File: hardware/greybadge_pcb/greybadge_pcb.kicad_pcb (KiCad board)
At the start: 2 copper layers, 105.3 x 99 mm, 64 parts, among them J1 CONN_01X14, J2 CONN_01X14, J3 USB_OTG, J4 Conn_02x08_Odd_Even, J5 Conn_02x03_Odd_Even, SW1 SW_Push, SW3 SW_Push, U1 iCE40-LP8K-CM81, U2 MIC5504-3.3YM5-TR, U3 DSC6001CI2A-016.0000T, U4 MIC5365-1.2YC5-TR, U5 AT25SF081-SSHD-B

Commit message: feat: linking tinyfpga stuff
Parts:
- C10: value 100nF -> 1uF
- C14: value 10nF -> 100nF
- C15: value 10nF -> 1uF
- C2, C3, C4: value 1uF -> 100nF
- C7, C9: value 100nF -> 10nF
- R1: value 1.5k -> 100
- R2: value 68 -> 1.5k
- R4: value 100 -> 68
- R5: value 10k -> 270
- R8: value 270 -> 10k
- U2: value MIC5504-3.3YM5-TR -> MIC5365-1.2YC5-TR
- moved C1 20.2 mm to (201.6, 79.9)
- moved C11 20.2 mm to (193.1, 90.1)
- moved C12 20.2 mm to (193.1, 90.9)
- moved C13 20.2 mm to (200.1, 90.2)
- moved C14 20.2 mm to (199.8, 88.4)
- moved C15 20.2 mm to (196.8, 87.0)
- moved C16 20.2 mm to (196.2, 94.4)
- moved C2 20.2 mm to (201.6, 83.5)
- moved C3 20.2 mm to (201.6, 85.9)
- moved C4 20.2 mm to (201.6, 82.3)
- moved C6 20.2 mm to (197.4, 96.1)
- moved C7 20.2 mm to (197.4, 93.7)
- moved C8 20.2 mm to (194.5, 93.8)
- moved C9 20.2 mm to (198.9, 93.5)
- moved D2 20.2 mm to (191.9, 79.4)
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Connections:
- C1 pad 1: (no net) -> +5V
- C1 pad 2: (no net) -> GND
- C10 pad 1: (no net) -> +3V3
- C10 pad 2: (no net) -> GND
- C11 pad 1: (no net) -> Net-(U3G-GNDPLL0)
- C11 pad 2: (no net) -> Net-(U3G-VCCPLL0)
- C12 pad 1: (no net) -> +3V3
- C12 pad 2: (no net) -> GND
- C13 pad 1: (no net) -> +3V3
- C13 pad 2: (no net) -> GND
- C14 pad 1: (no net) -> +3V3
- C14 pad 2: (no net) -> GND
- C15 pad 1: (no net) -> +1V2
- C15 pad 2: (no net) -> GND
- C16 pad 1: (no net) -> +3V3
- C16 pad 2: (no net) -> GND
- C2 pad 1: (no net) -> +3V3
- C2 pad 2: (no net) -> GND
- C3 pad 1: (no net) -> +3V3
- C3 pad 2: (no net) -> GND
- C4 pad 1: (no net) -> +1V2
- C4 pad 2: (no net) -> GND
- C7 pad 1: (no net) -> +1V2
- C7 pad 2: (no net) -> GND
- C9 pad 1: (no net) -> +1V2
- C9 pad 2: (no net) -> GND
- D1 pad 1: (no net) -> Net-(D1-K)
- D1 pad 2: (no net) -> +3V3
- D2 pad 1: (no net) -> Net-(D2-K)
- D2 pad 2: (no net) -> LED
- L1 pad 1: (no net) -> +5V
- L1 pad 2: (no net) -> Net-(J1-VBUS)
- R1 pad 1: (no net) -> Net-(U3G-VCCPLL0)
- R1 pad 2: (no net) -> +1V2
- R10 pad 1: (no net) -> +3V3
- R10 pad 2: (no net) -> SS
- R2 pad 1: (no net) -> Net-(J1-D+)
- R2 pad 2: (no net) -> USB_PU
- R3 pad 1: (no net) -> USB_P
- R3 pad 2: (no net) -> Net-(J1-D+)
- R4 pad 1: (no net) -> USB_N
- R4 pad 2: (no net) -> Net-(J1-D-)
- R5 pad 1: (no net) -> Net-(D1-K)
- R5 pad 2: (no net) -> GND
- R7 pad 1: (no net) -> +3V3
- R7 pad 2: (no net) -> 82
- R8 pad 1: (no net) -> +3V3
- R8 pad 2: (no net) -> 109
- SW1 pad 1: (no net) -> GND
- SW1 pad 2: (no net) -> CRESET_B
- TP1 pad 1: (no net) -> +1V2
- TP2 pad 1: (no net) -> 82
- TP3 pad 1: (no net) -> CRESET_B
- U2 pad 1: (no net) -> +3V3
- U2 pad 2: (no net) -> GND
- U2 pad 3: (no net) -> +3V3
- U2 pad 4: (no net) -> unconnected-(U2-NC-Pad4)
- U2 pad 5: (no net) -> +1V2
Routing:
- net (no net): track 699.3 -> 547.5 mm, vias 77 -> 41
- net GND: track 0.00 -> 43.9 mm, vias 0 -> 16
- net +1V2: track 0.00 -> 23.0 mm, vias 0 -> 3
- net SS: track 0.00 -> 20.3 mm, vias 0 -> 2
- net Net-(J1-D+): track 0.00 -> 17.0 mm, vias 0 -> 1
- net USB_P: track 0.00 -> 15.6 mm, vias 0 -> 1
- net LED: track 0.00 -> 13.4 mm, vias 0 -> 1
- net +3V3: track 0.00 -> 11.6 mm, vias 0 -> 8
- net Net-(J1-VBUS): track 0.00 -> 2.36 mm
- net Net-(D1-K): track 0.00 -> 1.84 mm, vias 0 -> 1
- net Net-(D2-K): track 0.00 -> 1.04 mm
- net Net-(U3G-VCCPLL0): track 0.00 -> 0.71 mm, vias 0 -> 1
- net 109: track 0.00 -> 0.63 mm, vias 0 -> 1
- net Net-(J1-D-): track 0.00 -> 0.42 mm, vias 0 -> 1
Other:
- board size 105.3 x 99 mm -> 124 x 99 mm

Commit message: feat: arrangement
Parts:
- moved J5 43.9 mm to (239.4, 77.4)
- moved C1 43.9 mm to (245.5, 78.5)
- moved C10 43.9 mm to (238.1, 81.9)
- moved C11 43.9 mm to (237.0, 88.7)
- moved C12 43.9 mm to (237.0, 89.5)
- moved C13 43.9 mm to (243.9, 88.7)
- moved C14 43.9 mm to (243.6, 87.0)
- moved C15 43.9 mm to (240.7, 85.5)
- moved C16 43.9 mm to (240.1, 93.0)
- moved C17 43.9 mm to (245.6, 75.5)
- moved C2 43.9 mm to (245.5, 82.1)
- moved C3 43.9 mm to (245.5, 84.5)
- moved C4 43.9 mm to (245.5, 80.9)
- moved C6 43.9 mm to (241.3, 94.7)
- moved C7 43.9 mm to (241.3, 92.2)
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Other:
- board size 124 x 99 mm -> 167.8 x 99 mm

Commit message: Update sch and pcb
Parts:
- added C18: 100n, Capacitor_SMD:C_0402_1005Metric, B.Cu at (94.1, 62.9)
- added C19: 4.7u, Capacitor_SMD:C_0402_1005Metric, B.Cu at (105.2, 61.9)
- added C20: 4.7u, Capacitor_SMD:C_0402_1005Metric, B.Cu at (103.5, 64.3)
- added C21: 4.7u, Capacitor_SMD:C_0402_1005Metric, B.Cu at (104.5, 64.3)
- added C22: 22pF, Capacitor_SMD:C_0402_1005Metric, B.Cu at (86.0, 68.7)
- added C23: 22pF, Capacitor_SMD:C_0402_1005Metric, B.Cu at (85.7, 65.2)
- added C24: 100n, Capacitor_SMD:C_0402_1005Metric, B.Cu at (106.0, 68.5)
- added C25: 100n, Capacitor_SMD:C_0402_1005Metric, B.Cu at (92.4, 68.8)
- added C26: 100n, Capacitor_SMD:C_0402_1005Metric, B.Cu at (97.7, 71.8)
- added C27: 100n, Capacitor_SMD:C_0402_1005Metric, B.Cu at (128.8, 53.5)
- added C28: 100n, Capacitor_SMD:C_0402_1005Metric, B.Cu at (110.7, 69.4)
- added C29: 100n, Capacitor_SMD:C_0402_1005Metric, B.Cu at (98.6, 61.0)
- added C30: 100n, Capacitor_SMD:C_0402_1005Metric, B.Cu at (102.7, 71.3)
- added C31: 100n, Capacitor_SMD:C_0402_1005Metric, B.Cu at (99.6, 61.0)
- added C32: 4.7u, Capacitor_SMD:C_0402_1005Metric, B.Cu at (99.7, 71.8)
- added C33: 100n, Capacitor_SMD:C_0402_1005Metric, B.Cu at (92.4, 66.2)
- added C34: 10u, Capacitor_SMD:C_0805_2012Metric, B.Cu at (130.5, 58.5)
- added C35: 10u, Capacitor_SMD:C_0805_2012Metric, B.Cu at (130.5, 55.5)
- added J6: SM03B-SRSS-TB, Connector_JST:JST_SH_SM03B-SRSS-TB_1x03-1MP_P1.00mm_Horizontal, B.Cu at (93.4, 46.3)
- added J7: USB_C_Receptacle_USB2.0, Connector_USB:USB_C_Receptacle_HRO_TYPE-C-31-M-12, B.Cu at (151.9, 61.1)
- added L2: 3.3u, footprints:L_pol_2016, B.Cu at (106.0, 64.3)
- added R11: DNF, Resistor_SMD:R_0402_1005Metric, B.Cu at (112.5, 78.7)
- added R12: 33, Resistor_SMD:R_0402_1005Metric, B.Cu at (104.0, 61.9)
- added R13: DNF, Resistor_SMD:R_0402_1005Metric, B.Cu at (112.5, 79.9)
- added R14: 0, Resistor_SMD:R_0402_1005Metric, B.Cu at (109.6, 80.0)
- added R15: 27R, Resistor_SMD:R_0402_1005Metric, B.Cu at (106.0, 67.1)
- added R16: 27R, Resistor_SMD:R_0402_1005Metric, B.Cu at (106.0, 66.1)
- added R17: 1k, Resistor_SMD:R_0402_1005Metric, B.Cu at (109.6, 81.2)
- added R18: 1k, Resistor_SMD:R_0402_1005Metric, B.Cu at (89.2, 65.5)
- added R19: 1k, Resistor_SMD:R_0402_1005Metric, B.Cu at (87.3, 62.5)
- added R20: 5k1, Resistor_SMD:R_0402_1005Metric, B.Cu at (144.8, 57.1)
- added R21: 5k1, Resistor_SMD:R_0402_1005Metric, B.Cu at (144.8, 65.3)
- added SW2: SW_Push, Button_Switch_SMD:SW_Push_1P1T_NO_Vertical_Wuerth_434133025816, B.Cu at (105.6, 83.0)
- added SW3: SW_Push, Button_Switch_SMD:SW_Push_1P1T_NO_Vertical_Wuerth_434133025816, B.Cu at (89.8, 59.9)
- added U6: W25Q128JVS, Package_SO:SOIC-8_5.3x5.3mm_P1.27mm, B.Cu at (108.3, 74.6)
- added U7: RP2350_60QFN, footprints:RP2350-QFN-60-1EP_7x7_P0.4mm_EP3.4x3.4mm_ThermalVias, B.Cu at (98.9, 66.5)
- added U8: NCP1117-3.3_SOT223, Package_TO_SOT_SMD:SOT-223-3_TabPin2, B.Cu at (137.7, 56.5)
- added Y1: 12Mhz, Crystal:Crystal_SMD_3225-4Pin_3.2x2.5mm, B.Cu at (87.6, 67.1)
- L1: footprint Inductors_SMD:L_0603 -> Inductor_SMD:L_0603_1608Metric
- renumbered C4 to C10, C7 to C11, C9 to C12, C12 to C13, C13 to C14, C14 to C15, C11 to C17, C15 to C3, C1 to C4, C10 to C6, C16 to C7, C2 to C8, C3 to C9, R2 to R1, R1 to R10, R3 to R2, R4 to R3, R5 to R4, R10 to R6, U2 to U4
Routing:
- net /rp2350/USB_D+: track 0.00 -> 43.5 mm
- net /rp2350/USB_D-: track 0.00 -> 43.3 mm
- net GND: track 43.9 -> 66.2 mm, vias 16 -> 25
- net /rp2350/GPIO0: track 0.00 -> 21.8 mm, vias 0 -> 2
- net +3V3: track 11.6 -> 31.3 mm, vias 8 -> 9
- net /rp2350/QSPI_SS: track 0.00 -> 17.0 mm
- net /rp2350/QSPI_SD1: track 0.00 -> 16.7 mm
- net /rp2350/QSPI_SD2: track 0.00 -> 12.5 mm
- net +1V1: track 0.00 -> 12.0 mm, vias 0 -> 5
- net /rp2350/XIN: track 0.00 -> 10.3 mm
- net /rp2350/QSPI_SD3: track 0.00 -> 8.64 mm
- net /rp2350/QSPI_SCLK: track 0.00 -> 7.19 mm
- net /rp2350/~{USB_BOOT}: track 0.00 -> 6.89 mm
- net (no net): track 547.5 -> 540.8 mm, vias 41 -> 40
- net /rp2350/XOUT: track 0.00 -> 6.34 mm
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- added copper zone on B.Cu, net +1V1
- added copper zone on B.Cu, net +3V3

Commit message: Update routing
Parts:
- moved C27 28.5 mm to (101.3, 61.0), turned to 90 degrees
- moved C34 9.96 mm to (140.5, 57.6), turned to 90 degrees
- moved U8 3.87 mm to (133.8, 56.5), turned to 180 degrees
- moved R19 2.94 mm to (85.7, 60.0), turned to 90 degrees
- moved C35 2.53 mm to (128.0, 55.6), turned to 90 degrees
- moved R21 2.27 mm to (144.5, 63.1)
- moved R20 2.17 mm to (144.5, 59.3)
- moved C18 2.15 mm to (95.3, 61.1)
- moved C26 1.35 mm to (97.4, 73.1)
- moved C32 1.34 mm to (100.0, 73.1)
- moved C30 0.91 mm to (103.5, 71.8), turned to -90 degrees
- moved SW3 0.65 mm to (89.4, 59.4), turned to 0 degrees
- moved C29 0.57 mm to (98.6, 60.5)
- moved C31 0.57 mm to (99.6, 60.5)
- moved C25 0.27 mm to (92.1, 68.8)
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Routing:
- net GND: track 66.2 -> 101.1 mm, vias 25 -> 38
- net VBUS: track 0.00 -> 17.9 mm, vias 0 -> 2
- net +3V3: track 31.3 -> 44.2 mm
- net /rp2350/RUN: track 2.90 -> 14.6 mm
- net /rp2350/GPIO16: track 0.00 -> 11.4 mm
- net /rp2350/GPIO17: track 0.00 -> 11.3 mm
- net +1V1: track 12.0 -> 22.9 mm, vias 5 -> 8
- net /rp2350/GPIO18: track 0.00 -> 10.1 mm
- net /rp2350/GPIO8: track 0.00 -> 7.39 mm
- net /rp2350/GPIO9: track 0.00 -> 6.83 mm
- net Net-(R19-Pad1): track 0.00 -> 5.91 mm
- net /rp2350/GPIO1: track 0.00 -> 5.85 mm
- net /rp2350/GPIO2: track 0.00 -> 5.81 mm
- net /rp2350/GPIO3: track 0.00 -> 5.63 mm
- net /rp2350/GPIO6: track 0.00 -> 5.53 mm
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- added copper zone on B.Cu, net GND
- added copper zone on F.Cu, net GND
- added copper zone on B.Cu, net VBUS

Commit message: Add screen
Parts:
- added C36: 100n, Capacitor_SMD:C_0402_1005Metric, B.Cu at (147.0, 116.0)
- added C37: 10u, Capacitor_SMD:C_0805_2012Metric, B.Cu at (147.8, 117.5)
- GC9A1: footprint Maibadge_Howard:GC9A01 -> footprints:GC9A01
- moved C35 0.77 mm to (128.8, 55.7)
- moved U8 0.77 mm to (134.5, 56.7)
- moved C34 0.19 mm to (140.4, 57.8)
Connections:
- GC9A1 pad 1: (no net) -> /rp2350/OLED_RST
- GC9A1 pad 2: (no net) -> /rp2350/OLED_CS
- GC9A1 pad 3: (no net) -> /rp2350/OLED_DC
- GC9A1 pad 4: (no net) -> /rp2350/OLED_SDA
- GC9A1 pad 5: (no net) -> /rp2350/OLED_SCL
- GC9A1 pad 6: (no net) -> GND
- GC9A1 pad 7: (no net) -> +3V3
- U7 pad 4: /rp2350/GPIO2 -> /rp2350/OLED_SCL
- U7 pad 5: /rp2350/GPIO3 -> /rp2350/OLED_SDA
- U7 pad 7: /rp2350/GPIO4 -> /rp2350/OLED_DC
- U7 pad 8: /rp2350/GPIO5 -> /rp2350/OLED_CS
- U7 pad 9: /rp2350/GPIO6 -> /rp2350/OLED_RST
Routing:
- net /rp2350/OLED_RST: track 0.00 -> 81.9 mm
- net /rp2350/OLED_CS: track 0.00 -> 80.4 mm
- net /rp2350/OLED_SCL: track 0.00 -> 79.3 mm
- net /rp2350/OLED_SDA: track 0.00 -> 78.9 mm
- net /rp2350/OLED_DC: track 0.00 -> 78.9 mm
- net +3V3: track 44.2 -> 81.9 mm
- net /rp2350/GPIO2: track 5.81 -> 0.00 mm
- net /rp2350/GPIO3: track 5.63 -> 0.00 mm
- net /rp2350/GPIO6: track 5.53 -> 0.00 mm
- net /rp2350/GPIO5: track 5.45 -> 0.00 mm
- net /rp2350/GPIO4: track 5.33 -> 0.00 mm
- net GND: track 101.1 -> 104.6 mm, vias 38 -> 41
- net VBUS: track 17.9 -> 17.2 mm

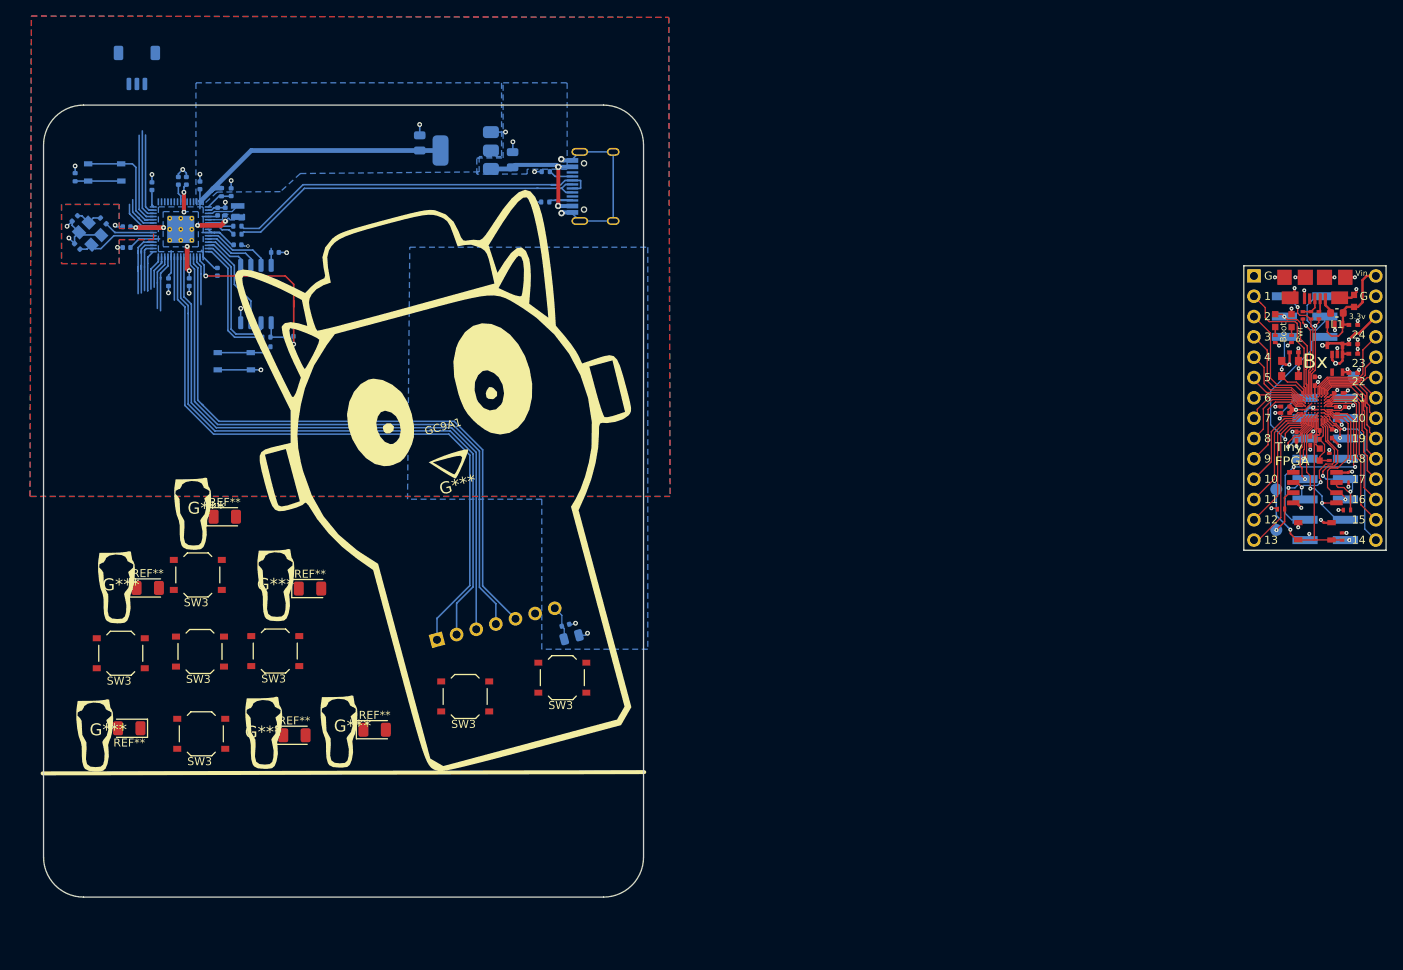
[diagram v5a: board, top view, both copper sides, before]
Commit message: Update routing and zones
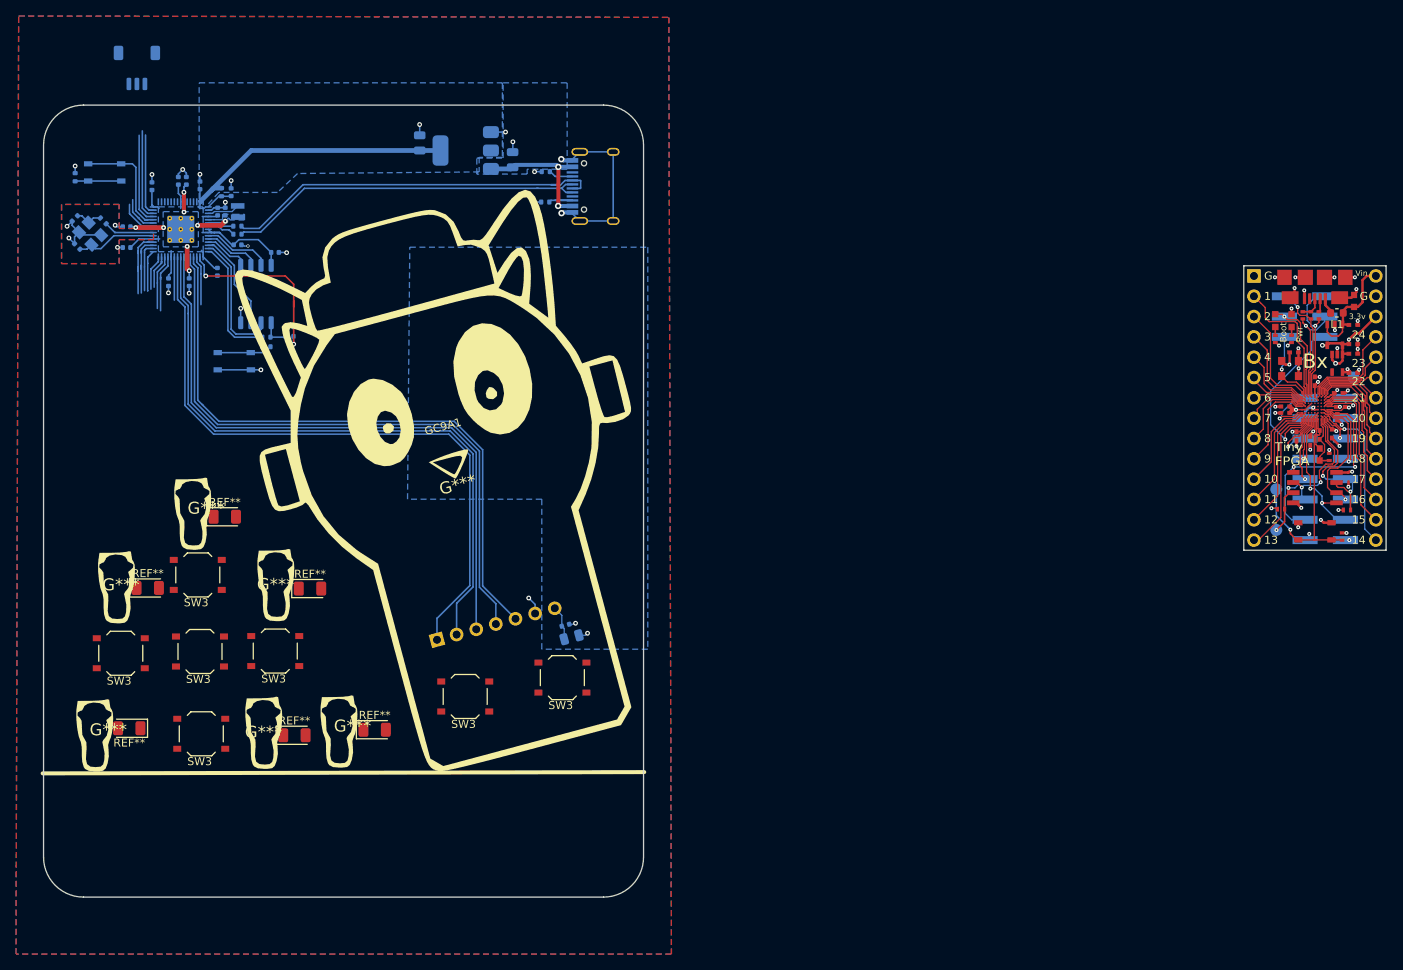
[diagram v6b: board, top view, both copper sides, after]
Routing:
- net +3V3: track 81.9 -> 88.7 mm
- net GND: track 104.6 -> 106.9 mm, vias 41 -> 42
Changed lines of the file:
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@@
 	)
 	(via
+		(at 142.4 112.6)
+		(size 0.6)
+		(drill 0.3)
+		(layers "F.Cu" "B.Cu")
+		(net 1)
+	)
+	(via
 		(at 246.019862 77.961493)
 		(size 0.5)
@@
 	)
 	(segment
+		(start 143.196548 113.396548)
+		(end 142.4 112.6)
+		(width 0.2)
+		(layer "B.Cu")
+		(net 1)
+	)
+	(segment
 		(start 103.054644 63.81)
 		(end 103.510589 63.81)
@@
 	)
 	(segment
+		(start 143.196548 114.5374)
+		(end 143.196548 113.396548)
+		(width 0.2)
+		(layer "B.Cu")
+		(net 1)
+	)
+	(segment
 		(start 147.864999 64.4)
 		(end 147.864999 64.555001)
@@
 	(segment
 		(start 95.462499 63.712499)
+		(end 96.012499 63.712499)
+		(width 0.2)
+		(layer "B.Cu")
+		(net 3)
+	)
+	(segment
+		(start 95.462499 63.712499)
 		(end 95.462499 63.637501)
 		(width 0.2)
@@
 	)
 	(segment
+		(start 96.012499 63.712499)
+		(end 96.2 63.9)
+		(width 0.2)
+		(layer "B.Cu")
+		(net 3)
+	)
+	(segment
 		(start 102.3375 66.912499)
 		(end 103.082499 66.912499)
@@
 	)
 	(segment
+		(start 106.17 67.8)
+		(end 108.6 67.8)
+		(width 0.2)
+		(layer "B.Cu")
+		(net 3)
+	)
+	(segment
+		(start 108.6 67.8)
+		(end 110.2 69.4)
+		(width 0.2)
+		(layer "B.Cu")
+		(net 3)
+	)
+	(segment
+		(start 105.52 68.45)
+		(end 106.17 67.8)
+		(width 0.2)
+		(layer "B.Cu")
+		(net 3)
+	)
+	(segment
 		(start 110.205 71.0125)
 		(end 110.205 69.405)
@@
 	)
 	(segment
-		(start 110.2 69.4)
-		(end 110.2 68.9)
-		(width 0.2)
-		(layer "B.Cu")
-		(net 3)
-	)
-	(segment
 		(start 97.699999 69.949999)
 		(end 97.699999 71.939999)
@@
 	)
 	(segment
+		(start 98.9 63.074998)
+		(end 98.9 63.9)
+		(width 0.2)
+		(layer "B.Cu")
+		(net 3)
+	)
+	(segment
 		(start 98.9 62.33)
 		(end 98.6 62.03)
@@
 		(polygon
 			(pts
-				(xy 80.23 39.85) (xy 159.9 40.02) (xy 160.07 99.9) (xy 80.06 99.9)
+				(xy 78.6385 39.846604) (xy 159.9 40.02) (xy 160.232391 157.1) (xy 78.306558 157.1)
 			)
 		)
@@
 		(polygon
 			(pts
-				(xy 113.850916 59.536481) (xy 111.357943 61.80282) (xy 103.453266 61.853122) (xy 101.778768 63.366916)
-				(xy 100.801038 63.366916) (xy 100.801038 48.2) (xy 139 48.2) (xy 139 57.42) (xy 136.201038 57.42)
-				(xy 136.201038 59.335128)
+				(xy 113.5 59.536481) (xy 111 61.9) (xy 103.65345 61.9) (xy 101.843473 63.9) (xy 101.2 63.9) (xy 101.201038 48.2)
+				(xy 139.1 48.2) (xy 139.1 57.52) (xy 136.201038 57.52) (xy 136.201038 59.335128)
 			)
 		)

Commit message: Update routing/zones
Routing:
- net +3V3: track 88.7 -> 89.3 mm
- net GND: vias 42 -> 43
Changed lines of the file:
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@@
 	)
 	(via
+		(at 110.2 73.2)
+		(size 0.6)
+		(drill 0.3)
+		(layers "F.Cu" "B.Cu")
+		(free yes)
+		(net 1)
+	)
+	(via
 		(at 107.3 68.6)
 		(size 0.4)
@@
 	)
 	(segment
+		(start 105.52 68.45)
+		(end 106.17 67.8)
+		(width 0.2)
+		(layer "B.Cu")
+		(net 3)
+	)
+	(segment
 		(start 95.462499 63.637501)
 		(end 95.3 63.475002)
@@
 	)
 	(segment
-		(start 106.17 67.8)
-		(end 108.6 67.8)
-		(width 0.2)
-		(layer "B.Cu")
-		(net 3)
-	)
-	(segment
-		(start 108.6 67.8)
-		(end 110.2 69.4)
-		(width 0.2)
-		(layer "B.Cu")
-		(net 3)
-	)
-	(segment
-		(start 105.52 68.45)
-		(end 106.17 67.8)
-		(width 0.2)
-		(layer "B.Cu")
-		(net 3)
-	)
-	(segment
 		(start 110.205 71.0125)
 		(end 110.205 69.405)
@@
 	)
 	(segment
+		(start 109.6 67.8)
+		(end 110.2 68.4)
+		(width 0.2)
+		(layer "B.Cu")
+		(net 3)
+	)
+	(segment
 		(start 97.699999 69.949999)
 		(end 97.699999 69.189999)
@@
 	)
 	(segment
+		(start 110.2 68.4)
+		(end 110.2 69.4)
+		(width 0.2)
+		(layer "B.Cu")
+		(net 3)
+	)
+	(segment
 		(start 92.61 68.79)
 		(end 93.6875 67.7125)
@@
 	)
 	(segment
+		(start 106.17 67.8)
+		(end 109.6 67.8)
+		(width 0.2)
+		(layer "B.Cu")
+		(net 3)
+	)
+	(segment
 		(start 102.787499 61.587499)
 		(end 101.401 62.973999)
@@
 		(polygon
 			(pts
-				(xy 127.529018 68.75) (xy 157.279018 68.75) (xy 157.279018 119) (xy 144.029018 119) (xy 144.029018 100.25)
+				(xy 127.430093 79.3) (xy 112.5 79.3) (xy 112.5 70.4) (xy 110 70.4) (xy 110 68.95) (xy 105 68.95)
+				(xy 105 67.55) (xy 157.249887 67.55) (xy 157.279018 119) (xy 144.029018 119) (xy 144.029018 100.25)
 				(xy 127.247766 100.25)
 			)

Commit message: feat: fpga schematic
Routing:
- net USB_P: track 15.6 -> 22.7 mm
- net (no net): track 540.8 -> 533.7 mm
